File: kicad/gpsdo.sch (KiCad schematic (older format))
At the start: 41 parts, among them J1 Conn_Coaxial, J2 Conn_01x04_Male, J3 Conn_01x04_Male, J4 Conn_01x04_Male, J5 Conn_01x04_Male, J6 Conn_01x04_Male, U1 MSP430F5171IDA, U10 74AUC1G79, U2 MAX-8Q, U3 549CAAC000111BBG, U4 Si7051-A20, U5 LTC4317, U6 74LVC1G08, U7 74LVC1G08, U8 74AUC1G79, U9 74LVC1G86

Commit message: create gerber files
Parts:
- added R10: 47k, Resistor_SMD:R_0603_1608Metric, symbol Device:R_Small_US
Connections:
- net +3V3: now also R10.1
- net SBWTDIO: now also R10.2
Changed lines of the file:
@@
 Text Label 9450 6200 0    50   ~ 0
 CLK
+$Comp
+L Device:R_Small_US R10
+U 1 1 6101D1B0
+P 9550 850
+F 0 "R10" V 9345 850 50  0000 C CNN
+F 1 "47k" V 9436 850 50  0000 C CNN
+F 2 "Resistor_SMD:R_0603_1608Metric" H 9550 850 50  0001 C CNN
+F 3 "~" H 9550 850 50  0001 C CNN
+	1    9550 850
+	0    -1   1    0
+$EndComp
+Wire Wire Line
+	9650 850  9700 850
+Connection ~ 9700 850
+$Comp
+L power:+3.3V #PWR?
+U 1 1 6102115A
+P 9450 850
+F 0 "#PWR?" H 9450 700 50  0001 C CNN
+F 1 "+3.3V" V 9450 1100 50  0000 C CNN
+F 2 "" H 9450 850 50  0001 C CNN
+F 3 "" H 9450 850 50  0001 C CNN
+	1    9450 850
+	0    -1   1    0
+$EndComp
 $EndSCHEMATC

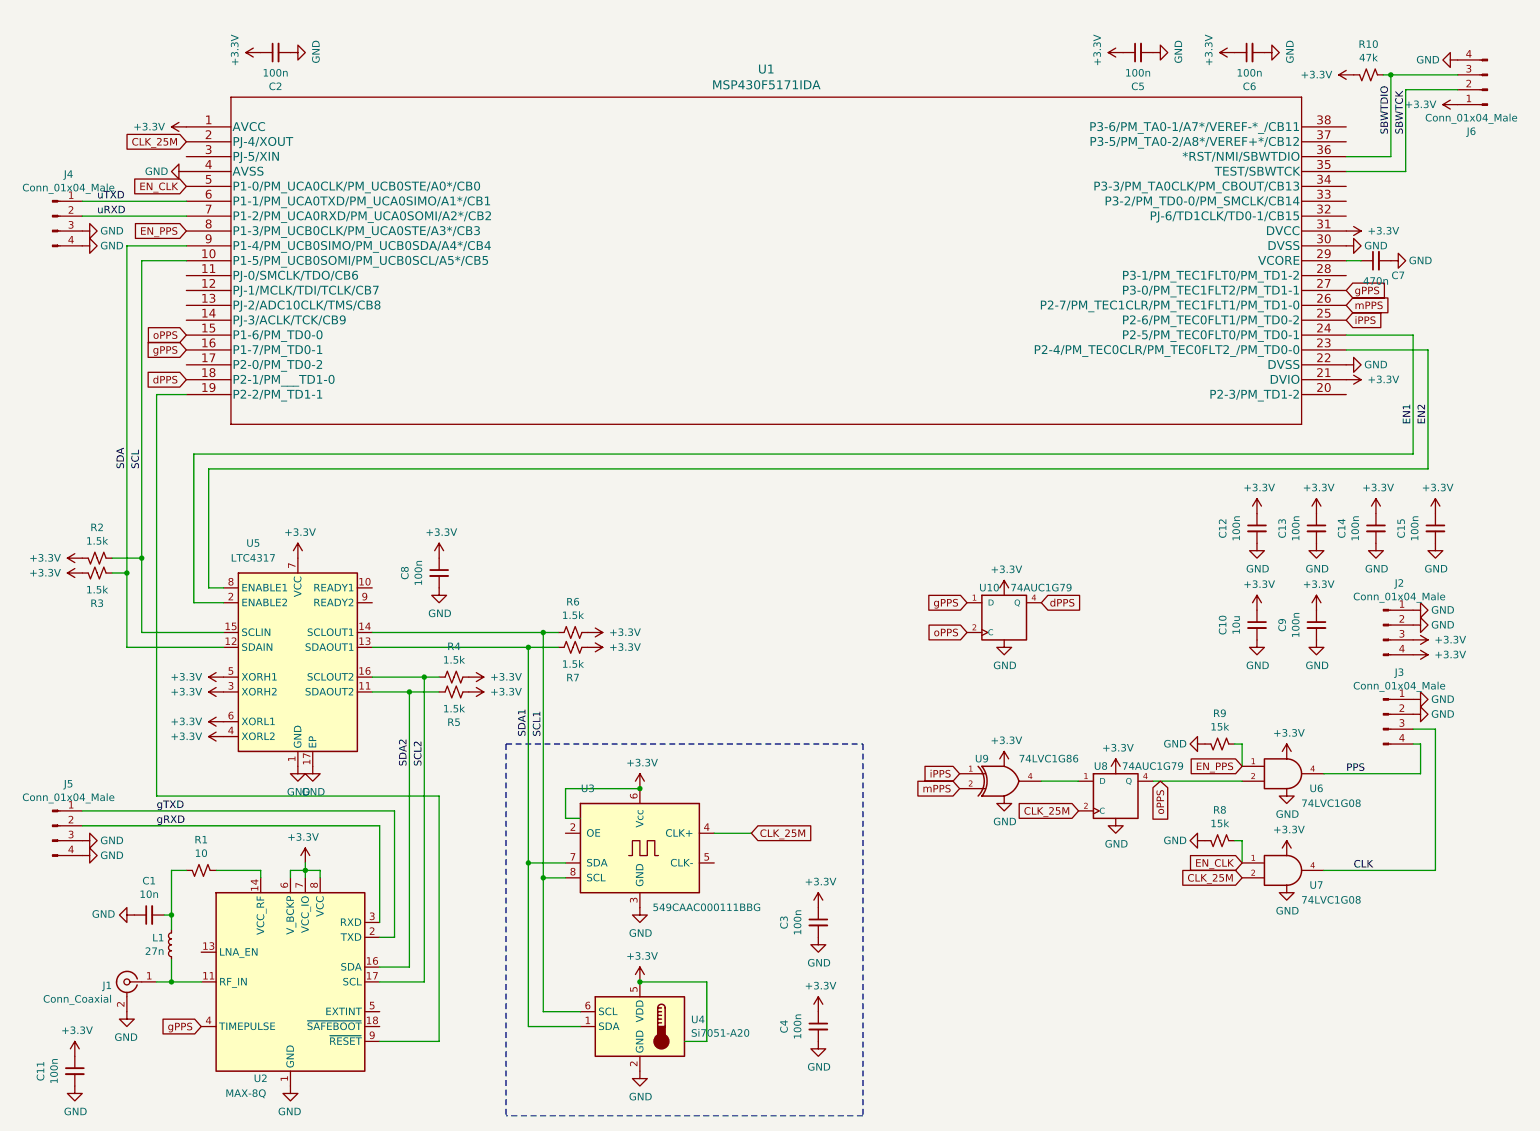
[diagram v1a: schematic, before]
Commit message: add DCXO shield
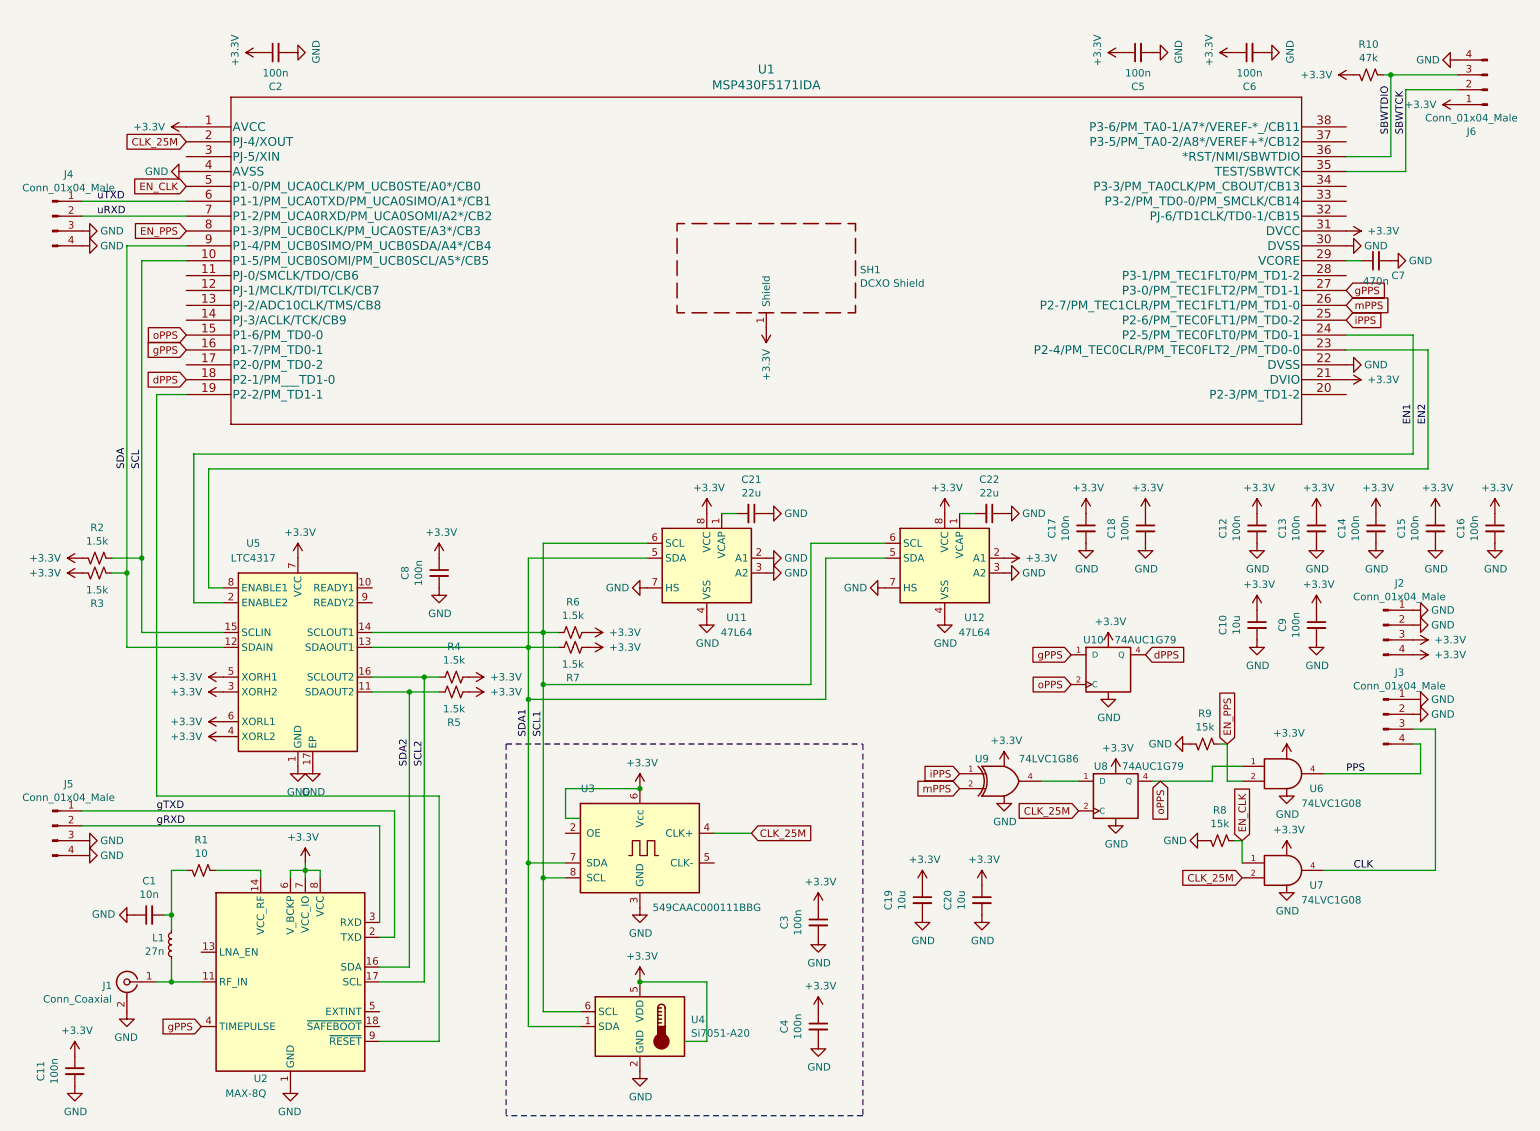
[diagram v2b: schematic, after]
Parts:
- added C16, C17, C18: 100n, Resistor_SMD:R_0603_1608Metric, symbol Device:C_Small
- added C19, C20: 10u, Capacitor_SMD:C_0805_2012Metric, symbol Device:C_Small
- added C21, C22: 22u, Capacitor_SMD:C_0805_2012Metric, symbol Device:C_Small
- added SH1: DCXO Shield, RF_Shielding:Laird_Technologies_BMI-S-102_16.50x16.50mm, symbol Device:RF_Shield_One_Piece
- added U11, U12: 47L64, Package_SO:SOIC-8_3.9x4.9mm_P1.27mm, symbol Memory_NVRAM:47L16
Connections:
- net +3V3: now also C16.1, C17.1, C18.1, C19.1, C20.1, SH1.1 (Shield), U11.8 (VCC), U12.2 (A1), U12.8 (VCC)
- net EN_PPS: now also U6.2; no longer U6.1
- net GND: now also C16.2, C17.2, C18.2, C19.2, C20.2, C21.1, C22.1, U11.2 (A1), U11.3 (A2), U11.4 (VSS), U11.7 (HS), U12.3 (A2), U12.4 (VSS), U12.7 (HS)
- net SCL1: now also U11.6 (SCL), U12.6 (SCL)
- net SDA1: now also U11.5 (SDA), U12.5 (SDA)
- net oPPS: now also U6.1; no longer U6.2
- new net: C21.2, U11.1 (VCAP)
- new net: C22.2, U12.1 (VCAP)
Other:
- moved on the sheet: R9, U10

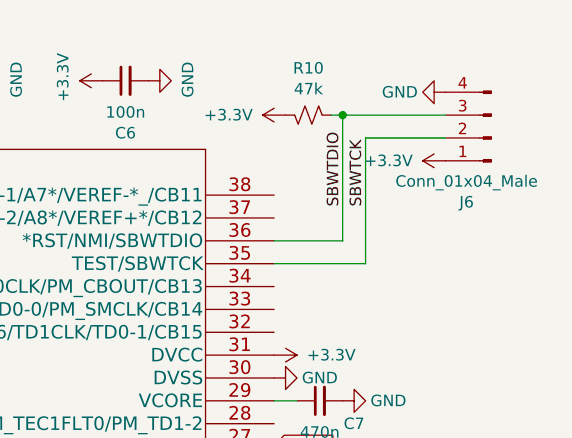
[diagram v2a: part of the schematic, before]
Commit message: fix SBW connection
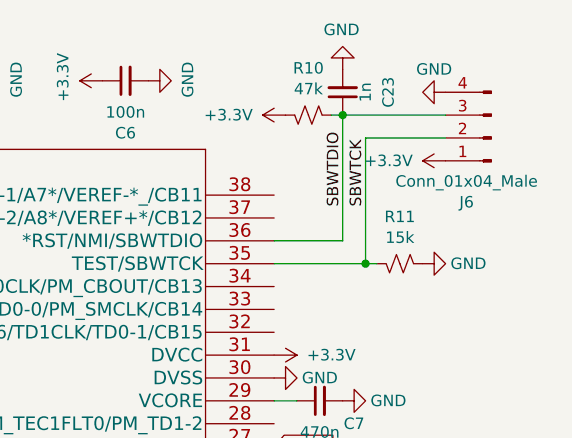
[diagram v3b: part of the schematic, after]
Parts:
- added C23: 1n, Resistor_SMD:R_0603_1608Metric, symbol Device:C_Small
- added R11: 15k, Resistor_SMD:R_0603_1608Metric, symbol Device:R_Small_US
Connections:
- net GND: now also C23.2, R11.2
- net SBWTCK: now also R11.1
- net SBWTDIO: now also C23.1
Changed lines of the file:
@@
 P 10150 750
 F 0 "#PWR0152" H 10150 500 50  0001 C CNN
-F 1 "GND" V 10150 550 50  0000 C CNN
+F 1 "GND" V 10050 700 50  0000 C CNN
 F 2 "" H 10150 750 50  0001 C CNN
 F 3 "" H 10150 750 50  0001 C CNN
@@
 $EndComp
 $Comp
-L power:+3.3V #PWR?
+L power:+3.3V #PWR0177
 U 1 1 610E291C
 P 5500 2550
-F 0 "#PWR?" H 5500 2400 50  0001 C CNN
+F 0 "#PWR0177" H 5500 2400 50  0001 C CNN
 F 1 "+3.3V" V 5500 2800 50  0000 C CNN
 F 2 "" H 5500 2550 50  0001 C CNN
@@
 	-1   0    0    1
 $EndComp
+$Comp
+L Device:R_Small_US R11
+U 1 1 61086ABE
+P 9950 1500
+F 0 "R11" V 9745 1500 50  0000 C CNN
+F 1 "15k" V 9836 1500 50  0000 C CNN
+F 2 "Resistor_SMD:R_0603_1608Metric" H 9950 1500 50  0001 C CNN
+F 3 "~" H 9950 1500 50  0001 C CNN
+	1    9950 1500
+	0    -1   1    0
+$EndComp
+$Comp
+L power:GND #PWR0178
+U 1 1 610870A0
+P 10050 1500
+F 0 "#PWR0178" H 10050 1250 50  0001 C CNN
+F 1 "GND" V 10050 1300 50  0000 C CNN
+F 2 "" H 10050 1500 50  0001 C CNN
+F 3 "" H 10050 1500 50  0001 C CNN
+	1    10050 1500
+	0    -1   -1   0
+$EndComp
+Wire Wire Line
+	9850 1500 9800 1500
+Connection ~ 9800 1500
+$Comp
+L Device:C_Small C23
+U 1 1 610AF32A
+P 9700 750
+F 0 "C23" V 9500 750 50  0000 C CNN
+F 1 "1n" V 9600 750 50  0000 C CNN
+F 2 "Resistor_SMD:R_0603_1608Metric" H 9700 750 50  0001 C CNN
+F 3 "~" H 9700 750 50  0001 C CNN
+	1    9700 750
+	-1   0    0    1
+$EndComp
+$Comp
+L power:GND #PWR0179
+U 1 1 610CC665
+P 9700 650
+F 0 "#PWR0179" H 9700 400 50  0001 C CNN
+F 1 "GND" H 9705 477 50  0000 C CNN
+F 2 "" H 9700 650 50  0001 C CNN
+F 3 "" H 9700 650 50  0001 C CNN
+	1    9700 650
+	-1   0    0    1
+$EndComp

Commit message: update pcb layout
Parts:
- removed C8: 100n, Resistor_SMD:R_0603_1608Metric, symbol Device:C_Small
- removed R4, R5, R6, R7: 1.5k, Resistor_SMD:R_0603_1608Metric, symbol Device:R_Small_US
- removed U5: LTC4317, Package_DFN_QFN:DFN-16-1EP_3x5mm_P0.5mm_EP1.66x4.4mm, symbol Interface:LTC4317
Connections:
- net SCL1 is gone; now on net SCL: U11.6 (SCL), U12.6 (SCL), U3.8 (SCL), U4.6 (SCL)
- net SCL2 is gone; now on net SCL: U2.17 (SCL)
- net SDA1 is gone; now on net SDA: U11.5 (SDA), U12.5 (SDA), U3.7 (SDA), U4.1 (SDA)
- net SDA2 is gone; now on net SDA: U2.16 (SDA)
- net GND: no longer U11.7 (HS)
- net EN1: no longer names the net of U1.24 (P2-5/PM_TEC0FLT0/PM_TD0-1)
- net EN2: no longer names the net of U1.23 (P2-4/PM_TEC0CLR/PM_TEC0FLT2_/PM_TD0-0)

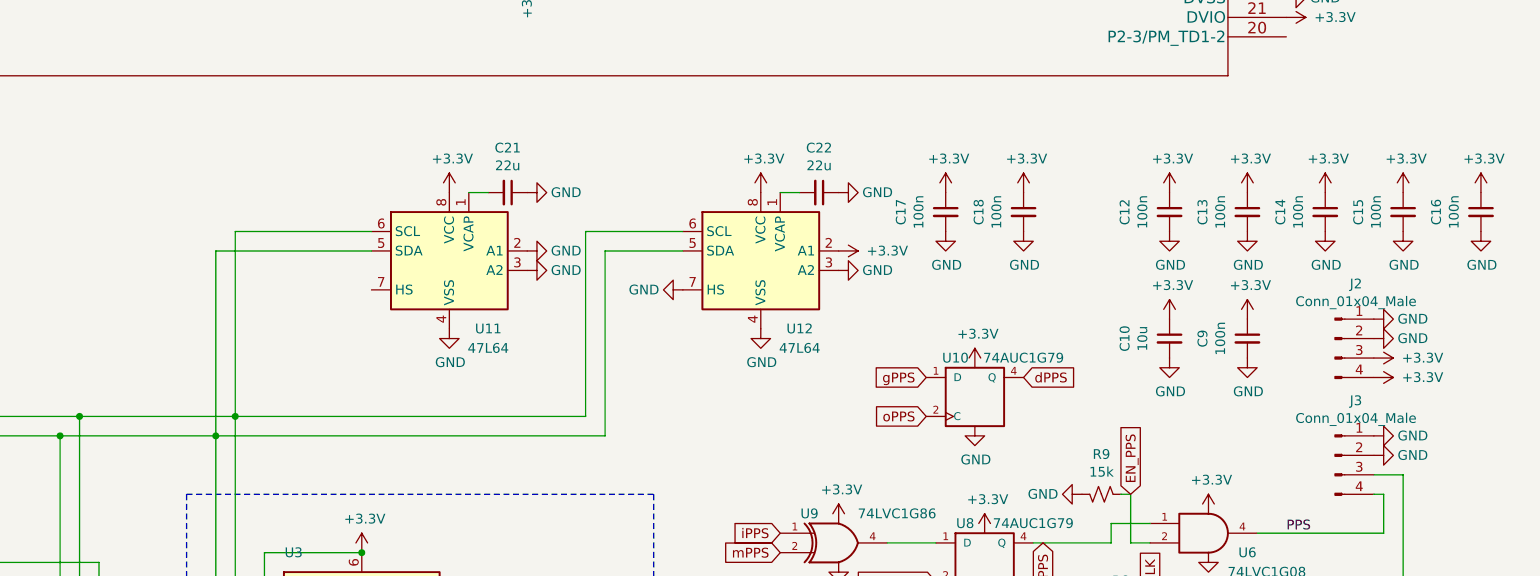
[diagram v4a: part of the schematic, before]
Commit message: remove extra EERAM
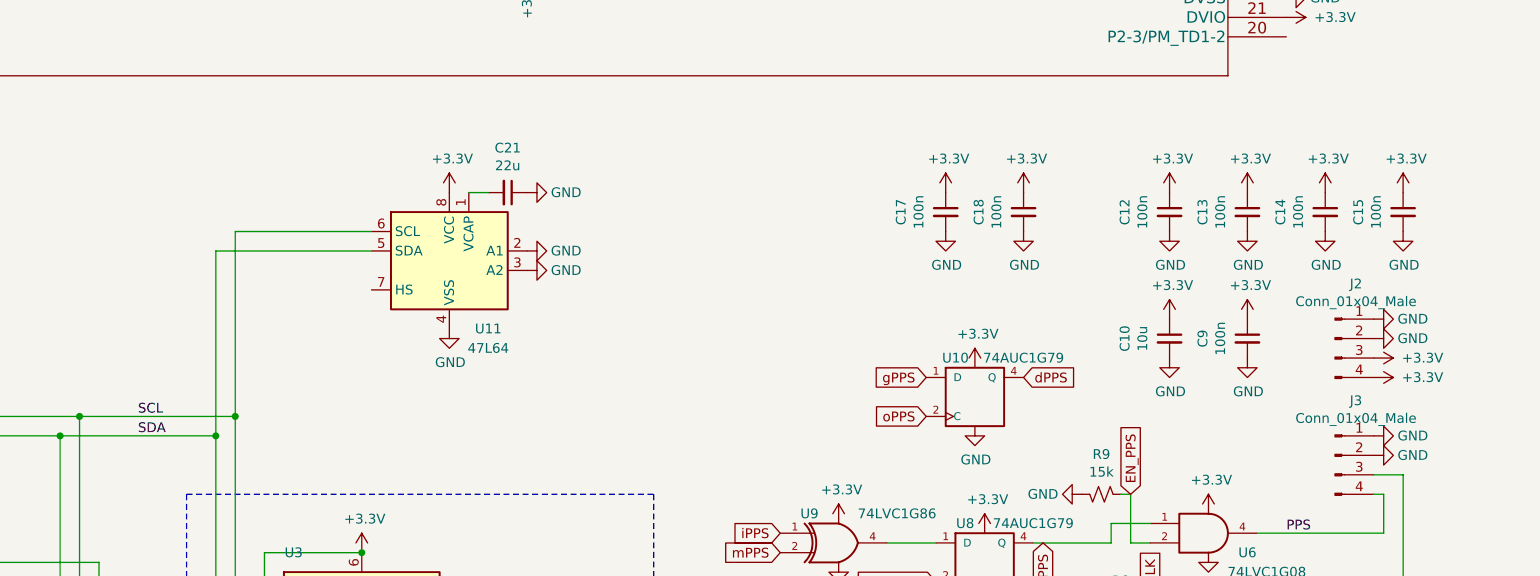
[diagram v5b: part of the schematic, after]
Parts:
- removed C16: 100n, Resistor_SMD:R_0603_1608Metric, symbol Device:C_Small
- removed C22: 22u, Capacitor_SMD:C_0805_2012Metric, symbol Device:C_Small
- removed U12: 47L64, Package_SO:SOIC-8_3.9x4.9mm_P1.27mm, symbol Memory_NVRAM:47L16
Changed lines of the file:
@@
 Wire Wire Line
 	4700 4000 4000 4000
-$Comp
-L Memory_NVRAM:47L16 U12
-U 1 1 6104EEB3
-P 6700 4100
-F 0 "U12" H 6900 3700 50  0000 C CNN
-F 1 "47L64" H 6900 3600 50  0000 C CNN
-F 2 "Package_SO:SOIC-8_3.9x4.9mm_P1.27mm" H 6700 3650 50  0001 C CNN
-F 3 "http://ww1.microchip.com/downloads/en/DeviceDoc/20005371C.pdf" H 6950 4450 50  0001 C CNN
-	1    6700 4100
-	1    0    0    -1
-$EndComp
-$Comp
-L power:GND #PWR0158
-U 1 1 6104EEB9
-P 6700 4500
-F 0 "#PWR0158" H 6700 4250 50  0001 C CNN
-F 1 "GND" H 6705 4327 50  0000 C CNN
-F 2 "" H 6700 4500 50  0001 C CNN
-F 3 "" H 6700 4500 50  0001 C CNN
-	1    6700 4500
-	1    0    0    -1
-$EndComp
-$Comp
-L power:+3.3V #PWR0159
-U 1 1 6104EEBF
-P 6700 3800
-F 0 "#PWR0159" H 6700 3650 50  0001 C CNN
-F 1 "+3.3V" H 6715 3973 50  0000 C CNN
-F 2 "" H 6700 3800 50  0001 C CNN
-F 3 "" H 6700 3800 50  0001 C CNN
-	1    6700 3800
-	1    0    0    -1
-$EndComp
-$Comp
-L power:GND #PWR0160
-U 1 1 6104EEC7
-P 6300 4300
-F 0 "#PWR0160" H 6300 4050 50  0001 C CNN
-F 1 "GND" V 6300 4100 50  0000 C CNN
-F 2 "" H 6300 4300 50  0001 C CNN
-F 3 "" H 6300 4300 50  0001 C CNN
-	1    6300 4300
-	0    1    1    0
-$EndComp
-Wire Wire Line
-	6300 4100 5900 4100
-Wire Wire Line
-	4000 4950 5800 4950
-Wire Wire Line
-	5800 4950 5800 4000
-Wire Wire Line
-	5800 4000 6300 4000
 Connection ~ 4000 4950
 Wire Wire Line
 	4000 4950 4000 6250
-Wire Wire Line
-	5900 5050 3900 5050
-Wire Wire Line
-	5900 4100 5900 5050
 Connection ~ 3900 5050
 Wire Wire Line
@@
 $EndComp
 $Comp
-L power:+3.3V #PWR0163
-U 1 1 6106253F
-P 7100 4100
-F 0 "#PWR0163" H 7100 3950 50  0001 C CNN
-F 1 "+3.3V" V 7100 4350 50  0000 C CNN
-F 2 "" H 7100 4100 50  0001 C CNN
-F 3 "" H 7100 4100 50  0001 C CNN
-	1    7100 4100
-	0    1    -1   0
-$EndComp
-$Comp
-L power:GND #PWR0164
-U 1 1 61062E83
-P 7100 4200
-F 0 "#PWR0164" H 7100 3950 50  0001 C CNN
-F 1 "GND" V 7100 4000 50  0000 C CNN
-F 2 "" H 7100 4200 50  0001 C CNN
-F 3 "" H 7100 4200 50  0001 C CNN
-	1    7100 4200
-	0    -1   -1   0
-$EndComp
-$Comp
 L Device:C_Small C18
 U 1 1 6106FE9E
@@
 F 3 "" H 7650 3800 50  0001 C CNN
 	1    7650 3800
-	1    0    0    -1
-$EndComp
-$Comp
-L Device:C_Small C16
-U 1 1 6107BCFD
-P 10400 3900
-F 0 "C16" V 10171 3900 50  0000 C CNN
-F 1 "100n" V 10262 3900 50  0000 C CNN
-F 2 "Resistor_SMD:R_0603_1608Metric" H 10400 3900 50  0001 C CNN
-F 3 "~" H 10400 3900 50  0001 C CNN
-	1    10400 3900
-	1    0    0    -1
-$EndComp
-$Comp
-L power:GND #PWR0169
-U 1 1 6107BD03
-P 10400 4000
-F 0 "#PWR0169" H 10400 3750 50  0001 C CNN
-F 1 "GND" H 10405 3827 50  0000 C CNN
-F 2 "" H 10400 4000 50  0001 C CNN
-F 3 "" H 10400 4000 50  0001 C CNN
-	1    10400 4000
-	1    0    0    -1
-$EndComp
-$Comp
-L power:+3.3V #PWR0170
-U 1 1 6107BD09
-P 10400 3800
-F 0 "#PWR0170" H 10400 3650 50  0001 C CNN
-F 1 "+3.3V" H 10415 3973 50  0000 C CNN
-F 2 "" H 10400 3800 50  0001 C CNN
-F 3 "" H 10400 3800 50  0001 C CNN
-	1    10400 3800
 	1    0    0    -1
 $EndComp
@@
 $EndComp
 $Comp
-L Device:C_Small C22
-U 1 1 610A4BF8
-P 7000 3800
-F 0 "C22" V 6771 3800 50  0000 C CNN
-F 1 "22u" V 6862 3800 50  0000 C CNN
-F 2 "Capacitor_SMD:C_0805_2012Metric" H 7000 3800 50  0001 C CNN
-F 3 "~" H 7000 3800 50  0001 C CNN
-	1    7000 3800
-	0    1    1    0
-$EndComp
-$Comp
 L power:GND #PWR0175
 U 1 1 610A552B
@@
 	0    -1   -1   0
 $EndComp
-$Comp
-L power:GND #PWR0176
-U 1 1 610A5D9D
-P 7100 3800
-F 0 "#PWR0176" H 7100 3550 50  0001 C CNN
-F 1 "GND" V 7100 3600 50  0000 C CNN
-F 2 "" H 7100 3800 50  0001 C CNN
-F 3 "" H 7100 3800 50  0001 C CNN
-	1    7100 3800
-	0    -1   -1   0
-$EndComp
-Wire Wire Line
-	6900 3800 6800 3800
 Wire Wire Line
 	5300 3800 5200 3800
@@
 Wire Wire Line
 	3100 5050 1200 5050
+Text Label 3500 5050 0    50   ~ 0
+SDA
+Text Label 3500 4950 0    50   ~ 0
+SCL
 $EndSCHEMATC
